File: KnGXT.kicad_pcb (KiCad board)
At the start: 2 copper layers, 94 x 108.3 mm, 114 parts, among them J1 USB_C_ReceptacleUSB2.0, J2 Conn_01x10_Male, SW1 RotaryEncoder_Switch, SW10 SW_Push, SW11 SW_Push, SW12 SW_Push, SW13 SW_Push, SW14 SW_Push, SW15 SW_Push, SW16 SW_Push, SW17 SW_Push, SW2 RotaryEncoder_Switch, SW3 SW_Push, SW4 SW_Push, SW5 SW_Push, SW6 SW_Push, SW7 SW_Push, SW8 SW_Push, SW9 SW_Push, U1 AMS1117-3.3, U2 W25Q128JVS, U3 RP2040, U4 74125, Y1 12MHz

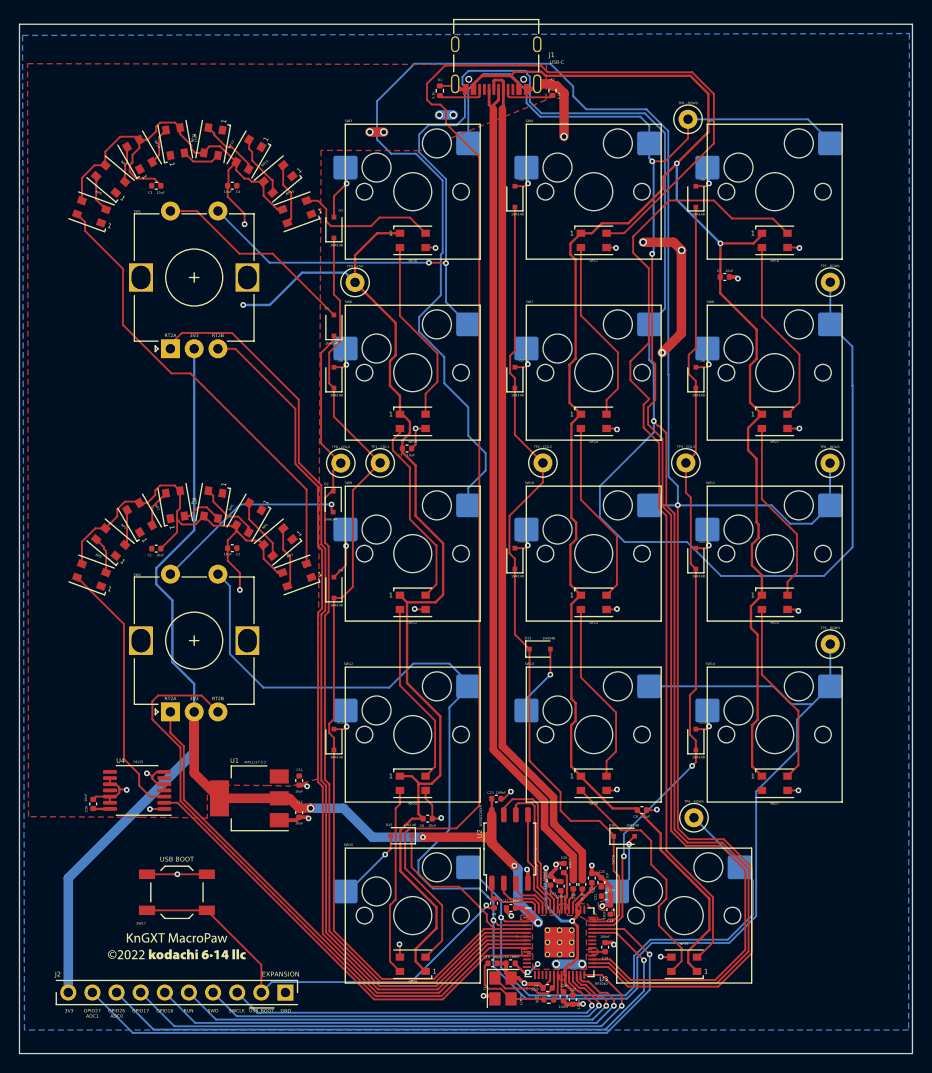
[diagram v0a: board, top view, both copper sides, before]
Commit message: Update the world to switch to 3.5x2.8mm WS2812B LEDs
Signed-off-by: Flynn <flynn+github@kodachi.com>
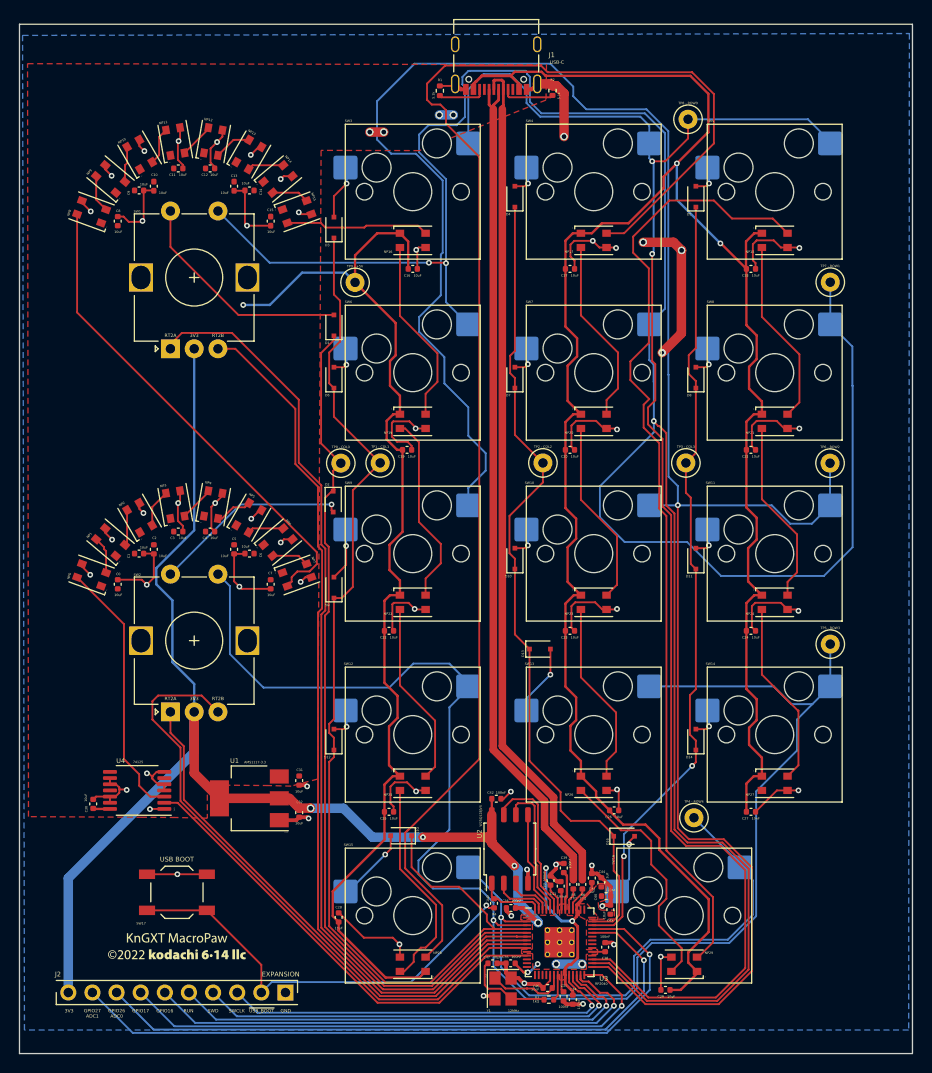
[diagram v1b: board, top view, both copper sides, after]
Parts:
- added C0: 10uF, Capacitor_SMD:C_0402_1005Metric, F.Cu at (27.7, 81.6)
- added C10: 10uF, Capacitor_SMD:C_0402_1005Metric, F.Cu at (31.5, 39.7)
- added C11: 10uF, Capacitor_SMD:C_0402_1005Metric, F.Cu at (34.1, 37.8)
- added C12: 10uF, Capacitor_SMD:C_0402_1005Metric, F.Cu at (37.5, 37.8)
- added C14: 10uF, Capacitor_SMD:C_0402_1005Metric, F.Cu at (41.6, 40.1)
- added C15: 10uF, Capacitor_SMD:C_0402_1005Metric, F.Cu at (43.8, 43.4)
- added C16: 10uF, Capacitor_SMD:C_0402_1005Metric, F.Cu at (58.8, 48.4)
- added C17: 10uF, Capacitor_SMD:C_0402_1005Metric, F.Cu at (75.3, 48.4)
- added C18: 10uF, Capacitor_SMD:C_0402_1005Metric, F.Cu at (94.4, 48.4)
- added C2: 10uF, Capacitor_SMD:C_0402_1005Metric, F.Cu at (31.5, 77.9)
- added C21: 10uF, Capacitor_SMD:C_0402_1005Metric, F.Cu at (94.4, 67.5)
- added C22: 10uF, Capacitor_SMD:C_0402_1005Metric, F.Cu at (56.3, 86.5)
- added C23: 10uF, Capacitor_SMD:C_0402_1005Metric, F.Cu at (75.3, 86.5)
- added C24: 10uF, Capacitor_SMD:C_0402_1005Metric, F.Cu at (94.4, 86.5)
- added C25: 10uF, Capacitor_SMD:C_0402_1005Metric, F.Cu at (56.3, 105.5)
- added C27: 10uF, Capacitor_SMD:C_0402_1005Metric, F.Cu at (94.4, 105.5)
- added C29: 10uF, Capacitor_SMD:C_0402_1005Metric, F.Cu at (85.4, 124.3)
- added C3: 10uF, Capacitor_SMD:C_0402_1005Metric, F.Cu at (34.1, 76.0)
- added C4: 10uF, Capacitor_SMD:C_0402_1005Metric, F.Cu at (37.5, 76.0)
- added C6: 10uF, Capacitor_SMD:C_0402_1005Metric, F.Cu at (41.6, 78.4)
- added C7: 10uF, Capacitor_SMD:C_0402_1005Metric, F.Cu at (43.8, 81.6)
- added C8: 10uF, Capacitor_SMD:C_0402_1005Metric, F.Cu at (27.7, 43.4)
- R3, R4: value 1k -> 1kΩ
- R5, R6: value 27 -> 27Ω
- U3: footprint RP2040_minimal:RP2040-QFN-56 -> RP_Silicon:RP2040-QFN-56
- moved C20 24.4 mm to (75.3, 67.5)
- moved C28 14.0 mm to (51.0, 116.7), turned to 90 degrees
- moved G*** 4.63 mm to (34.0, 115.0)
- moved C26 2.93 mm to (80.0, 105.4)
- moved C1 1.88 mm to (30.0, 78.4)
- moved C9 1.87 mm to (30.0, 40.1)
- moved C5 0.23 mm to (40.0, 77.9), turned to -90 degrees
- moved C13 0.20 mm to (40.0, 39.7), turned to -90 degrees
- moved C19 0.14 mm to (58.2, 67.5)
- turned NP12 to -100 degrees
- turned NP13 to -120 degrees
- turned NP14 to -140 degrees
- turned NP15 to -160 degrees
- turned NP4 to -100 degrees
- turned NP5 to -120 degrees
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- renumbered C4 to C13, C5 to C19, C7 to C20, C8 to C26, C6 to C28, C26 to C30, C11 to C31, C12 to C32, C14 to C33, C15 to C34, C16 to C35, C17 to C36, C18 to C37, C19 to C38, C20 to C39, C21 to C40, C22 to C41, C23 to C42, C24 to C43, C25 to C44, C13 to C45, C9 to C46, C10 to C47, C2 to C5, C3 to C9
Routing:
- net GND: track 199.1 -> 243.2 mm, vias 40 -> 57
- net +5V: track 335.9 -> 353.3 mm
- net Net-(NP7-Pad2): track 48.0 -> 51.6 mm
- net Net-(NP17-Pad4): track 155.9 -> 153.0 mm
- net Net-(NP13-Pad2): track 6.65 -> 3.81 mm
- net Net-(NP25-Pad2): track 19.9 -> 22.8 mm
- net Net-(NP4-Pad2): track 6.74 -> 3.96 mm
- net Net-(NP5-Pad2): track 6.58 -> 3.81 mm
- net Net-(NP14-Pad2): track 6.58 -> 3.92 mm
- net /ROW0: track 163.5 -> 166.2 mm
- net /ROW1: track 268.1 -> 270.8 mm
- net /ROW2: track 224.0 -> 226.6 mm
- net Net-(NP6-Pad2): track 6.50 -> 3.92 mm
- net Net-(NP12-Pad2): track 6.47 -> 3.96 mm
- net Net-(D1-Pad2): track 21.7 -> 24.0 mm
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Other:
- board text added: "All diodes are 1N4148, LCSC C2128"
- board text added: "All {dblquote}NP{dblquote} devices are WS28128B, LCSC C965557"
- board text added: "Keyswitches are hot-swappable Cherry-compatible"
- board text added: "U1 1"
- board text added: "U2 1"
- board text added: "U3 1"
- board text added: "U4 1"
- board text added: "Y1 1"

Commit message: Swap the WS2812B _AGAIN_ since the C965557 is out of stock
Thankfully the C2890364 is identical to the C965557, just
rotated 180 degrees.

Signed-off-by: Flynn <flynn+github@kodachi.com>
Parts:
- NP0, NP1, NP10, NP11, NP12, NP13, NP14, NP15, NP16, NP17, NP18, NP19, NP2, NP20, NP21, NP22, NP23, NP24, NP25, NP26, NP27, NP28, NP29, NP3, NP4, NP5, NP6, NP7, NP8, NP9: footprint LED_SMD:LED_WS2812B_PLCC4_3.5x2.8mm_P1.5mm -> LED_SMD:LED_WS2812B_3.5x2.8_C2890364
- R3, R4: value 1kΩ -> 1k
- R5, R6: value 27Ω -> 27
- turned NP0 to 160 degrees
- turned NP1 to 140 degrees
- turned NP10 to 120 degrees
- turned NP11 to 100 degrees
- turned NP12 to 80 degrees
- turned NP13 to 60 degrees
- turned NP14 to 40 degrees
- turned NP15 to 20 degrees
- turned NP16 to 0 degrees
- turned NP17 to 0 degrees
- turned NP18 to 0 degrees
- turned NP19 to 0 degrees
- turned NP2 to 120 degrees
- turned NP20 to 0 degrees
- turned NP21 to 0 degrees
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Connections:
- NP0 pad 1: +5V -> GND
- NP0 pad 2: Net-(NP0-Pad2) -> /NEOPXL
- NP0 pad 3: GND -> +5V
- NP0 pad 4: /NEOPXL -> Net-(NP0-Pad4)
- NP1 pad 1: +5V -> GND
- NP1 pad 2: Net-(NP1-Pad2) -> Net-(NP0-Pad4)
- NP1 pad 3: GND -> +5V
- NP1 pad 4: Net-(NP0-Pad2) -> Net-(NP1-Pad4)
- NP10 pad 1: +5V -> GND
- NP10 pad 3: GND -> +5V
- NP11 pad 1: +5V -> GND
- NP11 pad 2: Net-(NP11-Pad2) -> Net-(NP10-Pad4)
- NP11 pad 3: GND -> +5V
- NP11 pad 4: Net-(NP10-Pad2) -> Net-(NP11-Pad4)
- NP12 pad 1: +5V -> GND
- NP12 pad 2: Net-(NP12-Pad2) -> Net-(NP11-Pad4)
- NP12 pad 3: GND -> +5V
- NP12 pad 4: Net-(NP11-Pad2) -> Net-(NP12-Pad4)
- NP13 pad 1: +5V -> GND
- NP13 pad 2: Net-(NP13-Pad2) -> Net-(NP12-Pad4)
- NP13 pad 3: GND -> +5V
- NP13 pad 4: Net-(NP12-Pad2) -> Net-(NP13-Pad4)
- NP14 pad 1: +5V -> GND
- NP14 pad 2: Net-(NP14-Pad2) -> Net-(NP13-Pad4)
- NP14 pad 3: GND -> +5V
- NP14 pad 4: Net-(NP13-Pad2) -> Net-(NP14-Pad4)
- NP15 pad 1: +5V -> GND
- NP15 pad 2: Net-(NP15-Pad2) -> Net-(NP14-Pad4)
- NP15 pad 3: GND -> +5V
- NP15 pad 4: Net-(NP14-Pad2) -> Net-(NP15-Pad4)
- NP16 pad 1: +5V -> GND
- NP16 pad 2: Net-(NP16-Pad2) -> Net-(NP15-Pad4)
- NP16 pad 3: GND -> +5V
- NP16 pad 4: Net-(NP15-Pad2) -> Net-(NP16-Pad4)
- NP17 pad 1: +5V -> GND
- NP17 pad 3: GND -> +5V
- NP18 pad 1: +5V -> GND
- NP18 pad 3: GND -> +5V
- NP19 pad 1: +5V -> GND
- NP19 pad 2: Net-(NP19-Pad2) -> Net-(NP16-Pad4)
- NP19 pad 3: GND -> +5V
- NP19 pad 4: Net-(NP16-Pad2) -> Net-(NP19-Pad4)
- NP2 pad 1: +5V -> GND
- NP2 pad 2: Net-(NP2-Pad2) -> Net-(NP1-Pad4)
- NP2 pad 3: GND -> +5V
- NP2 pad 4: Net-(NP1-Pad2) -> Net-(NP2-Pad4)
- NP20 pad 1: +5V -> GND
- NP20 pad 2: Net-(NP20-Pad2) -> Net-(NP17-Pad4)
- NP20 pad 3: GND -> +5V
- NP20 pad 4: Net-(NP17-Pad2) -> Net-(NP20-Pad4)
- NP21 pad 1: +5V -> GND
- NP21 pad 2: Net-(NP21-Pad2) -> Net-(NP18-Pad4)
- NP21 pad 3: GND -> +5V
- NP21 pad 4: Net-(NP18-Pad2) -> Net-(NP21-Pad4)
- NP22 pad 1: +5V -> GND
- NP22 pad 2: Net-(NP22-Pad2) -> Net-(NP19-Pad4)
- NP22 pad 3: GND -> +5V
- NP22 pad 4: Net-(NP19-Pad2) -> Net-(NP22-Pad4)
- NP23 pad 1: +5V -> GND
- NP23 pad 2: Net-(NP23-Pad2) -> Net-(NP20-Pad4)
- NP23 pad 3: GND -> +5V
- NP23 pad 4: Net-(NP20-Pad2) -> Net-(NP23-Pad4)
- NP24 pad 1: +5V -> GND
- NP24 pad 2: Net-(NP24-Pad2) -> Net-(NP21-Pad4)
- NP24 pad 3: GND -> +5V
- NP24 pad 4: Net-(NP21-Pad2) -> Net-(NP24-Pad4)
- NP25 pad 1: +5V -> GND
- NP25 pad 2: Net-(NP25-Pad2) -> Net-(NP22-Pad4)
- NP25 pad 3: GND -> +5V
- NP25 pad 4: Net-(NP22-Pad2) -> Net-(NP25-Pad4)
- NP26 pad 1: +5V -> GND
- NP26 pad 2: Net-(NP26-Pad2) -> Net-(NP23-Pad4)
- NP26 pad 3: GND -> +5V
- NP26 pad 4: Net-(NP23-Pad2) -> Net-(NP26-Pad4)
- NP27 pad 1: +5V -> GND
- NP27 pad 2: unconnected-(NP27-Pad2) -> Net-(NP24-Pad4)
- NP27 pad 3: GND -> +5V
- NP27 pad 4: Net-(NP24-Pad2) -> unconnected-(NP27-Pad4)
- NP28 pad 1: +5V -> GND
- NP28 pad 2: Net-(NP17-Pad4) -> Net-(NP25-Pad4)
- NP28 pad 3: GND -> +5V
- NP28 pad 4: Net-(NP25-Pad2) -> Net-(NP17-Pad2)
- NP29 pad 1: +5V -> GND
- NP29 pad 2: Net-(NP18-Pad4) -> Net-(NP26-Pad4)
- NP29 pad 3: GND -> +5V
- NP29 pad 4: Net-(NP26-Pad2) -> Net-(NP18-Pad2)
- NP3 pad 1: +5V -> GND
- NP3 pad 2: Net-(NP3-Pad2) -> Net-(NP2-Pad4)
- NP3 pad 3: GND -> +5V
- NP3 pad 4: Net-(NP2-Pad2) -> Net-(NP3-Pad4)
- NP4 pad 1: +5V -> GND
- NP4 pad 2: Net-(NP4-Pad2) -> Net-(NP3-Pad4)
- NP4 pad 3: GND -> +5V
- NP4 pad 4: Net-(NP3-Pad2) -> Net-(NP4-Pad4)
- NP5 pad 1: +5V -> GND
- NP5 pad 2: Net-(NP5-Pad2) -> Net-(NP4-Pad4)
- NP5 pad 3: GND -> +5V
- NP5 pad 4: Net-(NP4-Pad2) -> Net-(NP5-Pad4)
- NP6 pad 1: +5V -> GND
- NP6 pad 2: Net-(NP6-Pad2) -> Net-(NP5-Pad4)
- NP6 pad 3: GND -> +5V
- NP6 pad 4: Net-(NP5-Pad2) -> Net-(NP6-Pad4)
- NP7 pad 1: +5V -> GND
- NP7 pad 2: Net-(NP7-Pad2) -> Net-(NP6-Pad4)
- NP7 pad 3: GND -> +5V
- NP7 pad 4: Net-(NP6-Pad2) -> Net-(NP7-Pad4)
- NP8 pad 1: +5V -> GND
- NP8 pad 2: Net-(NP8-Pad2) -> Net-(NP7-Pad4)
- NP8 pad 3: GND -> +5V
- NP8 pad 4: Net-(NP7-Pad2) -> Net-(NP8-Pad4)
- NP9 pad 1: +5V -> GND
- NP9 pad 2: Net-(NP10-Pad4) -> Net-(NP8-Pad4)
- NP9 pad 3: GND -> +5V
- NP9 pad 4: Net-(NP8-Pad2) -> Net-(NP10-Pad2)
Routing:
- net Net-(NP17-Pad4): track 153.0 -> 19.7 mm
- net Net-(NP17-Pad2): track 19.7 -> 153.0 mm
- net Net-(NP18-Pad4): track 101.5 -> 19.7 mm
- net Net-(NP18-Pad2): track 19.7 -> 101.5 mm
- net Net-(NP7-Pad4): track 0.00 -> 51.6 mm
- net Net-(NP7-Pad2): track 51.6 -> 0.00 mm
- net Net-(NP26-Pad4): track 0.00 -> 25.8 mm
- net Net-(NP26-Pad2): track 25.8 -> 0.00 mm
- net Net-(NP25-Pad4): track 0.00 -> 22.8 mm
- net Net-(NP25-Pad2): track 22.8 -> 0.00 mm
- net Net-(NP19-Pad4): track 0.00 -> 20.3 mm
- net Net-(NP19-Pad2): track 20.3 -> 0.00 mm
- net Net-(NP16-Pad4): track 0.00 -> 19.7 mm
- net Net-(NP16-Pad2): track 19.7 -> 0.00 mm
- net Net-(NP24-Pad4): track 0.00 -> 19.7 mm
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
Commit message: Add version number
Signed-off-by: Flynn <flynn+github@kodachi.com>
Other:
- board text added: "v0.1.0 – 20220813"
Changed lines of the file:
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@@
     (fp_line (start -3.5 3.5) (end -3.5 -2.5) (layer "F.Fab") (width 0.1))
     (fp_line (start 3.5 -3.5) (end 3.5 3.5) (layer "F.Fab") (width 0.1))
-    (pad "" smd roundrect locked (at 0.6375 0.6375) (size 1.084435 1.084435) (layers "F.Paste") (roundrect_rratio 0.230535))
-    (pad "" smd roundrect locked (at -0.6375 -0.6375) (size 1.084435 1.084435) (layers "F.Paste") (roundrect_rratio 0.230535))
-    (pad "" smd roundrect locked (at 0.6375 -0.6375) (size 1.084435 1.084435) (layers "F.Paste") (roundrect_rratio 0.230535))
-    (pad "" smd roundrect locked (at -0.6375 0.6375) (size 1.084435 1.084435) (layers "F.Paste") (roundrect_rratio 0.230535))
+    (pad "" smd roundrect locked (at 0.6375 0.6375) (size 1.084435 1.084435) (layers "F.Paste") (roundrect_rratio 0.2305347946))
+    (pad "" smd roundrect locked (at -0.6375 -0.6375) (size 1.084435 1.084435) (layers "F.Paste") (roundrect_rratio 0.2305347946))
+    (pad "" smd roundrect locked (at 0.6375 -0.6375) (size 1.084435 1.084435) (layers "F.Paste") (roundrect_rratio 0.2305347946))
+    (pad "" smd roundrect locked (at -0.6375 0.6375) (size 1.084435 1.084435) (layers "F.Paste") (roundrect_rratio 0.2305347946))
     (pad "1" smd roundrect locked (at -3.4375 -2.6) (size 0.875 0.2) (layers "F.Cu" "F.Paste" "F.Mask") (roundrect_rratio 0.25)
       (net 3 "+3V3") (pinfunction "IOVDD") (pintype "power_in"))
@@
     (effects (font (size 0.25 0.25) (thickness 0.0625)) (justify mirror))
   )
+  (gr_text "v0.1.0 – 20220813" (at 34.1 118.9) (layer "B.SilkS")
+    (effects (font (size 0.25 0.25) (thickness 0.0625)) (justify mirror))
+  )
   (gr_text "GND" (at 45.425 126.5) (layer "B.SilkS")
     (effects (font (size 0.35 0.35) (thickness 0.08)) (justify mirror))
@@
     (effects (font (size 0.35 0.35) (thickness 0.08)))
   )
+  (gr_text "v0.1.0 – 20220813" (at 33.975 121.9) (layer "F.SilkS")
+    (effects (font (size 0.25 0.25) (thickness 0.0625)))
+  )
   (gr_text "RT2A" (at 33.2928 55.4094) (layer "F.SilkS")
